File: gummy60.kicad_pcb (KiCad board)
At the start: 2 copper layers, 284.7 x 94.2 mm, 128 parts, among them J1 USB_C_Receptacle_USB2.0, SW1 CPG151101S11, SW10 CPG151101S11, SW11 CPG151101S11, SW12 CPG151101S11, SW13 CPG151101S11, SW14 CPG151101S11, SW2 CPG151101S11, SW20 CPG151101S11, SW21 CPG151101S11, SW22 CPG151101S11, SW23 CPG151101S11, SW24 CPG151101S11, SW25 CPG151101S11, SW26 CPG151101S11, SW27 CPG151101S11, SW28 CPG151101S11, SW29 CPG151101S11, SW3 CPG151101S11, SW30 CPG151101S11, SW31 CPG151101S11, SW32 CPG151101S11, SW33 CPG151101S11, SW34 CPG151101S11, SW35 CPG151101S11, SW36 CPG151101S11, SW37 CPG151101S11, SW38 CPG151101S11, SW39 CPG151101S11, SW4 CPG151101S11, SW40 CPG151101S11, SW41 CPG151101S11, SW42 CPG151101S11, SW43 CPG151101S11, SW44 CPG151101S11, SW45 CPG151101S11, SW46 CPG151101S11, SW47 CPG151101S11, SW48 CPG151101S11, SW49 CPG151101S11, SW5 CPG151101S11, SW50 CPG151101S11, SW51 CPG151101S11, SW52 CPG151101S11, SW53 CPG151101S11, SW54 CPG151101S11, SW55 CPG151101S11, SW56 CPG151101S11, SW57 CPG151101S11, SW58 CPG151101S11, SW59 CPG151101S11, SW6 CPG151101S11, SW60 CPG151101S11, SW61 CPG151101S11, SW62 CPG151101S11, SW63 CPG151101S11, SW64 CPG151101S11, SW65 CPG151101S11, SW66 CPG151101S11, SW67 CPG151101S11, SW68 CPG151101S11, SW69 CPG151101S11, SW7 CPG151101S11, SW70 CPG151101S11, SW71 CPG151101S11, SW72 CPG151101S11, SW73 CPG151101S11, SW74 CPG151101S11, SW75 CPG151101S11, SW76 CPG151101S11, SW77 CPG151101S11, SW8 CPG151101S11, SW81 CPG151101S11, SW82 CPG151101S11, SW83 CPG151101S11, SW84 CPG151101S11, SW85 CPG151101S11, SW86 CPG151101S11, SW9 SW_Push, U3 ATmega32U4-M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

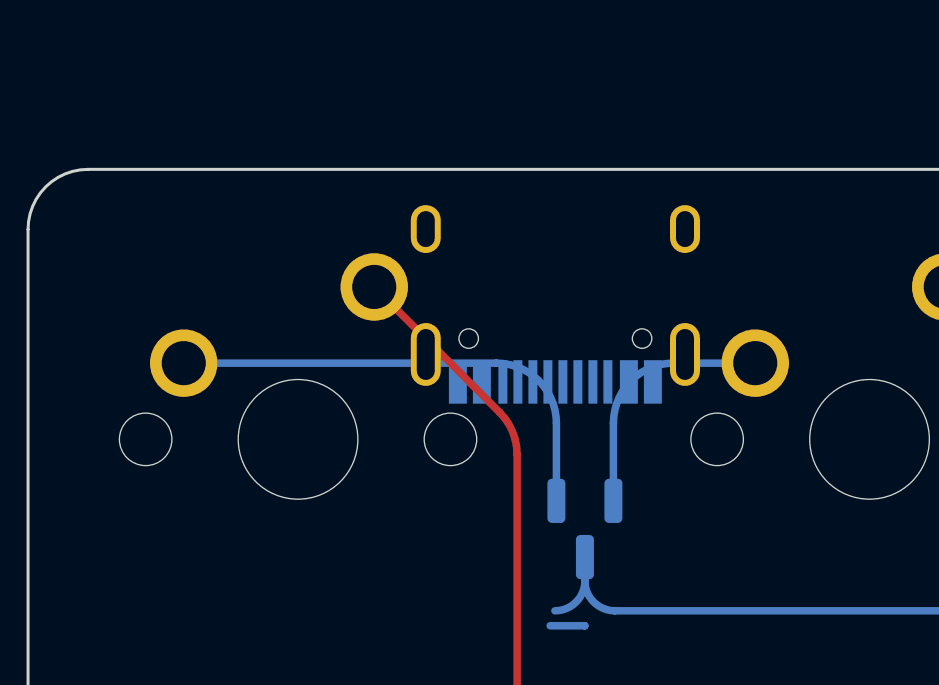
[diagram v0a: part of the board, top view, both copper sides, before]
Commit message: Properly placed usb
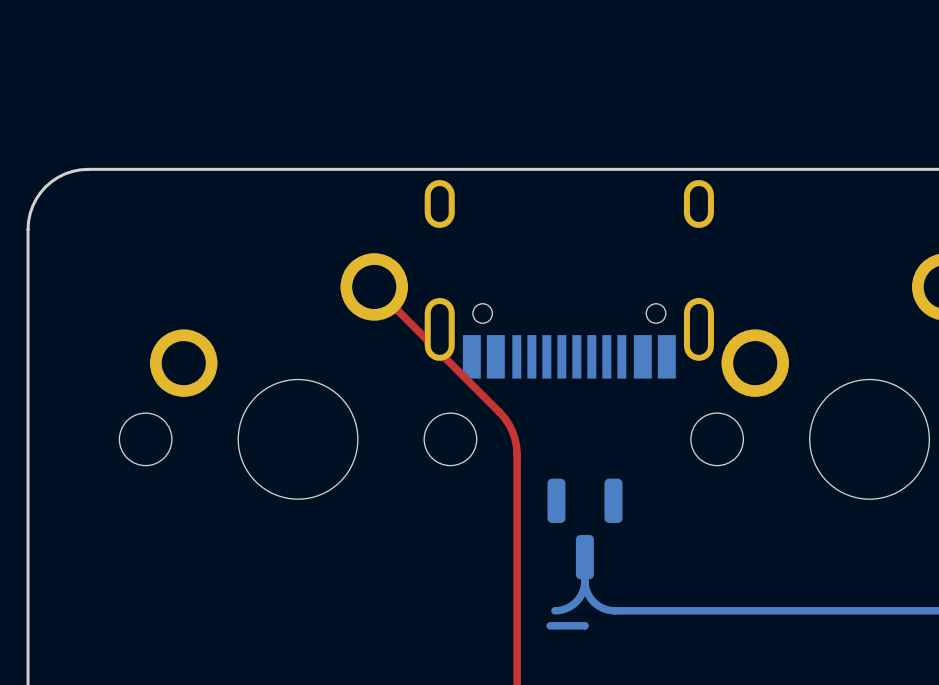
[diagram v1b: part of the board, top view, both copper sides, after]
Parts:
- J1: footprint Connector_USB:USB_C_Receptacle_HRO_TYPE-C-31-M-12 -> logo:USB_C_Receptacle_HRO_TYPE-C-31-M-12
- moved J1 0.96 mm to (60.5, 129.0)
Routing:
- net Net-(D1-Pad1): track 16.1 -> 0.00 mm
- net Net-(D1-Pad2): track 8.38 -> 0.00 mm
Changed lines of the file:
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@@
     (pad "" np_thru_hole circle locked (at 5.08 0 48.0996) (size 1.75 1.75) (drill 1.75) (layers *.Cu *.Mask))
     (pad "1" thru_hole circle locked (at -3.81 -2.54) (size 2.25 2.25) (drill 1.47) (layers *.Cu "B.Mask")
-      (net 81 "Net-(D1-Pad2)") (pinfunction "1") (pintype "passive"))
+      (net 81 "Net-(D1-Pad2)") (pinfunction "1"))
     (pad "2" thru_hole circle locked (at 2.54 -5.08) (size 2.25 2.25) (drill 1.47) (layers *.Cu "B.Mask")
-      (net 64 "C2") (pinfunction "2") (pintype "passive"))
+      (net 64 "C2") (pinfunction "2"))
   )
   (footprint "MX_Only:MXOnly-1U-NoLED" (layer "F.Cu")
@@
     )
   )
-  (footprint "Connector_USB:USB_C_Receptacle_HRO_TYPE-C-31-M-12" (layer "B.Cu")
-    (at 60.078222 129.853729)
+  (footprint "logo:USB_C_Receptacle_HRO_TYPE-C-31-M-12" (layer "B.Cu")
+    (at 60.543022 129.018029)
     (descr "USB Type-C receptacle for USB 2.0 and PD, http://www.krhro.com/uploads/soft/180320/1-1P320120243.pdf")
     (tags "usb usb-c 2.0 pd")
@@
     (fp_line (start -4.7 -3.9) (end 4.7 -3.9) (layer "B.SilkS") (width 0.12))
     (fp_line (start 4.7 1.9) (end 4.7 -0.1) (layer "B.SilkS") (width 0.12))
-    (fp_line (start -4.7 -2) (end -4.7 -3.9) (layer "B.SilkS") (width 0.12))
     (fp_line (start -4.7 1.9) (end -4.7 -0.1) (layer "B.SilkS") (width 0.12))
+    (fp_line (start -4.7 -2) (end -4.7 -3.9) (layer "B.SilkS") (width 0.12))
+    (fp_line (start -5.32 -4.15) (end 5.32 -4.15) (layer "B.CrtYd") (width 0.05))
     (fp_line (start -5.32 5.27) (end 5.32 5.27) (layer "B.CrtYd") (width 0.05))
-    (fp_line (start -5.32 5.27) (end -5.32 -4.15) (layer "B.CrtYd") (width 0.05))
     (fp_line (start 5.32 5.27) (end 5.32 -4.15) (layer "B.CrtYd") (width 0.05))
-    (fp_line (start -5.32 -4.15) (end 5.32 -4.15) (layer "B.CrtYd") (width 0.05))
-    (fp_line (start -4.47 -3.65) (end 4.47 -3.65) (layer "B.Fab") (width 0.1))
-    (fp_line (start -4.47 3.65) (end 4.47 3.65) (layer "B.Fab") (width 0.1))
+    (fp_line (start -5.32 5.27) (end -5.32 -4.15) (layer "B.CrtYd") (width 0.05))
     (fp_line (start -4.47 3.65) (end -4.47 -3.65) (layer "B.Fab") (width 0.1))
+    (fp_line (start -4.47 -3.65) (end 4.47 -3.65) (layer "B.Fab") (width 0.1))
     (fp_line (start 4.47 3.65) (end 4.47 -3.65) (layer "B.Fab") (width 0.1))
-    (pad "" np_thru_hole circle locked (at 2.89 2.6) (size 0.65 0.65) (drill 0.65) (layers *.Cu *.Mask))
+    (fp_line (start -4.47 3.65) (end 4.47 3.65) (layer "B.Fab") (width 0.1))
     (pad "" np_thru_hole circle locked (at -2.89 2.6) (size 0.65 0.65) (drill 0.65) (layers *.Cu *.Mask))
+    (pad "" np_thru_hole circle locked (at 2.89 2.6) (size 0.65 0.65) (drill 0.65) (layers *.Cu *.Mask))
     (pad "A1" smd rect locked (at -3.25 4.045) (size 0.6 1.45) (layers "B.Cu" "B.Paste" "B.Mask")
-      (net 55 "GND") (pinfunction "GND") (pintype "passive"))
+      (net 55 "GND") (pinfunction "GND"))
     (pad "A4" smd rect locked (at -2.45 4.045) (size 0.6 1.45) (layers "B.Cu" "B.Paste" "B.Mask")
-      (net 98 "VBUS") (pinfunction "VBUS") (pintype "passive"))
+      (net 98 "VBUS") (pinfunction "VBUS"))
     (pad "A5" smd rect locked (at -1.25 4.045) (size 0.3 1.45) (layers "B.Cu" "B.Paste" "B.Mask")
-      (net 102 "Net-(J1-PadA5)") (pinfunction "CC1") (pintype "bidirectional"))
+      (net 102 "Net-(J1-PadA5)") (pinfunction "CC1"))
     (pad "A6" smd rect locked (at -0.25 4.045) (size 0.3 1.45) (layers "B.Cu" "B.Paste" "B.Mask")
-      (net 7 "D+") (pinfunction "D+") (pintype "bidirectional"))
+      (net 7 "D+") (pinfunction "D+"))
     (pad "A7" smd rect locked (at 0.25 4.045) (size 0.3 1.45) (layers "B.Cu" "B.Paste" "B.Mask")
-      (net 6 "D-") (pinfunction "D-") (pintype "bidirectional"))
+      (net 6 "D-") (pinfunction "D-"))
     (pad "A8" smd rect locked (at 1.25 4.045) (size 0.3 1.45) (layers "B.Cu" "B.Paste" "B.Mask")
-      (net 100 "unconnected-(J1-PadA8)") (pinfunction "SBU1") (pintype "bidirectional+no_connect"))
+      (net 100 "unconnected-(J1-PadA8)") (pinfunction "SBU1"))
     (pad "A9" smd rect locked (at 2.45 4.045) (size 0.6 1.45) (layers "B.Cu" "B.Paste" "B.Mask")
-      (net 98 "VBUS") (pinfunction "VBUS") (pintype "passive"))
+      (net 98 "VBUS") (pinfunction "VBUS"))
     (pad "A12" smd rect locked (at 3.25 4.045) (size 0.6 1.45) (layers "B.Cu" "B.Paste" "B.Mask")
-      (net 55 "GND") (pinfunction "GND") (pintype "passive"))
+      (net 55 "GND") (pinfunction "GND"))
     (pad "B1" smd rect locked (at 3.25 4.045) (size 0.6 1.45) (layers "B.Cu" "B.Paste" "B.Mask")
-      (net 55 "GND") (pinfunction "GND") (pintype "passive"))
+      (net 55 "GND") (pinfunction "GND"))
     (pad "B4" smd rect locked (at 2.45 4.045) (size 0.6 1.45) (layers "B.Cu" "B.Paste" "B.Mask")
-      (net 98 "VBUS") (pinfunction "VBUS") (pintype "passive"))
+      (net 98 "VBUS") (pinfunction "VBUS"))
     (pad "B5" smd rect locked (at 1.75 4.045) (size 0.3 1.45) (layers "B.Cu" "B.Paste" "B.Mask")
-      (net 99 "Net-(J1-PadB5)") (pinfunction "CC2") (pintype "bidirectional"))
+      (net 99 "Net-(J1-PadB5)") (pinfunction "CC2"))
     (pad "B6" smd rect locked (at 0.75 4.045) (size 0.3 1.45) (layers "B.Cu" "B.Paste" "B.Mask")
-      (net 7 "D+") (pinfunction "D+") (pintype "bidirectional"))
+      (net 7 "D+") (pinfunction "D+"))
     (pad "B7" smd rect locked (at -0.75 4.045) (size 0.3 1.45) (layers "B.Cu" "B.Paste" "B.Mask")
-      (net 6 "D-") (pinfunction "D-") (pintype "bidirectional"))
+      (net 6 "D-") (pinfunction "D-"))
     (pad "B8" smd rect locked (at -1.75 4.045) (size 0.3 1.45) (layers "B.Cu" "B.Paste" "B.Mask")
-      (net 103 "unconnected-(J1-PadB8)") (pinfunction "SBU2") (pintype "bidirectional+no_connect"))
+      (net 103 "unconnected-(J1-PadB8)") (pinfunction "SBU2"))
     (pad "B9" smd rect locked (at -2.45 4.045) (size 0.6 1.45) (layers "B.Cu" "B.Paste" "B.Mask")
-      (net 98 "VBUS") (pinfunction "VBUS") (pintype "passive"))
+      (net 98 "VBUS") (pinfunction "VBUS"))
     (pad "B12" smd rect locked (at -3.25 4.045) (size 0.6 1.45) (layers "B.Cu" "B.Paste" "B.Mask")
-      (net 55 "GND") (pinfunction "GND") (pintype "passive"))
+      (net 55 "GND") (pinfunction "GND"))
+    (pad "S1" thru_hole oval locked (at -4.32 3.13) (size 1 2.1) (drill oval 0.6 1.7) (layers *.Cu *.Mask)
+      (net 55 "GND") (pinfunction "SHIELD"))
     (pad "S1" thru_hole oval locked (at 4.32 -1.05) (size 1 1.6) (drill oval 0.6 1.2) (layers *.Cu *.Mask)
-      (net 55 "GND") (pinfunction "SHIELD") (pintype "passive"))
+      (net 55 "GND") (pinfunction "SHIELD"))
     (pad "S1" thru_hole oval locked (at -4.32 -1.05) (size 1 1.6) (drill oval 0.6 1.2) (layers *.Cu *.Mask)
-      (net 55 "GND") (pinfunction "SHIELD") (pintype "passive"))
+      (net 55 "GND") (pinfunction "SHIELD"))
     (pad "S1" thru_hole oval locked (at 4.32 3.13) (size 1 2.1) (drill oval 0.6 1.7) (layers *.Cu *.Mask)
-      (net 55 "GND") (pinfunction "SHIELD") (pintype "passive"))
-    (pad "S1" thru_hole oval locked (at -4.32 3.13) (size 1 2.1) (drill oval 0.6 1.7) (layers *.Cu *.Mask)
-      (net 55 "GND") (pinfunction "SHIELD") (pintype "passive"))
-    (model "${KICAD6_3DMODEL_DIR}/Connector_USB.3dshapes/USB_C_Receptacle_HRO_TYPE-C-31-M-12.wrl"
-      (offset (xyz 0 0 0))
+      (net 55 "GND") (pinfunction "SHIELD"))
+    (model "C:/Users/Martin/Downloads/Unified-Daughterboard-master/Unified-Daughterboard-master/Design Resources/C3/HRO__TYPE-C-31-M-12.step"
+      (offset (xyz -4.46 -3.65 0))
       (scale (xyz 1 1 1))
-      (rotate (xyz 0 0 0))
+      (rotate (xyz 90 -180 180))
     )
   )
@@
   (segment (start 148.248222 247.936458) (end 148.248222 244.519918) (width 0.25) (layer "B.Cu") (net 65))
   (arc (start 148.248222 244.519918) (mid 149.126902 242.398598) (end 151.248222 241.519918) (width 0.25) (layer "B.Cu") (net 65))
-  (segment (start 47.69 133.273) (end 58.1125 133.273) (width 0.25) (layer "B.Cu") (net 66))
-  (segment (start 60.1125 137.8625) (end 60.1125 135.273) (width 0.25) (layer "B.Cu") (net 66))
-  (arc (start 60.1125 135.273) (mid 59.526714 133.858786) (end 58.1125 133.273) (width 0.25) (layer "B.Cu") (net 66))
   (segment (start 138.175 137.8625) (end 138.175 135.273) (width 0.25) (layer "B.Cu") (net 67))
   (segment (start 142.94 133.273) (end 140.175 133.273) (width 0.25) (layer "B.Cu") (net 67))
@@
   (segment (start 157.2275 171.373) (end 154.4625 171.373) (width 0.25) (layer "B.Cu") (net 80))
   (arc (start 154.4625 171.373) (mid 153.048286 171.958786) (end 152.4625 173.373) (width 0.25) (layer "B.Cu") (net 80))
-  (segment (start 62.0125 137.8625) (end 62.0125 135.273) (width 0.25) (layer "B.Cu") (net 81))
-  (segment (start 66.74 133.273) (end 64.0125 133.273) (width 0.25) (layer "B.Cu") (net 81))
-  (arc (start 62.0125 135.273) (mid 62.598286 133.858786) (end 64.0125 133.273) (width 0.25) (layer "B.Cu") (net 81))
   (segment (start 171.515 152.323) (end 181.9 152.323) (width 0.25) (layer "B.Cu") (net 82))
   (segment (start 183.9 156.7625) (end 183.9 154.323) (width 0.25) (layer "B.Cu") (net 82))
